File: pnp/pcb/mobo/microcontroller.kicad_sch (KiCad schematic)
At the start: 32 parts, among them J1 SWD Header, J32 BOOT_JUMPER, SW1 SW_Push, SW2 SW_Push, U1 STM32F407VETx, Y1 8MHz

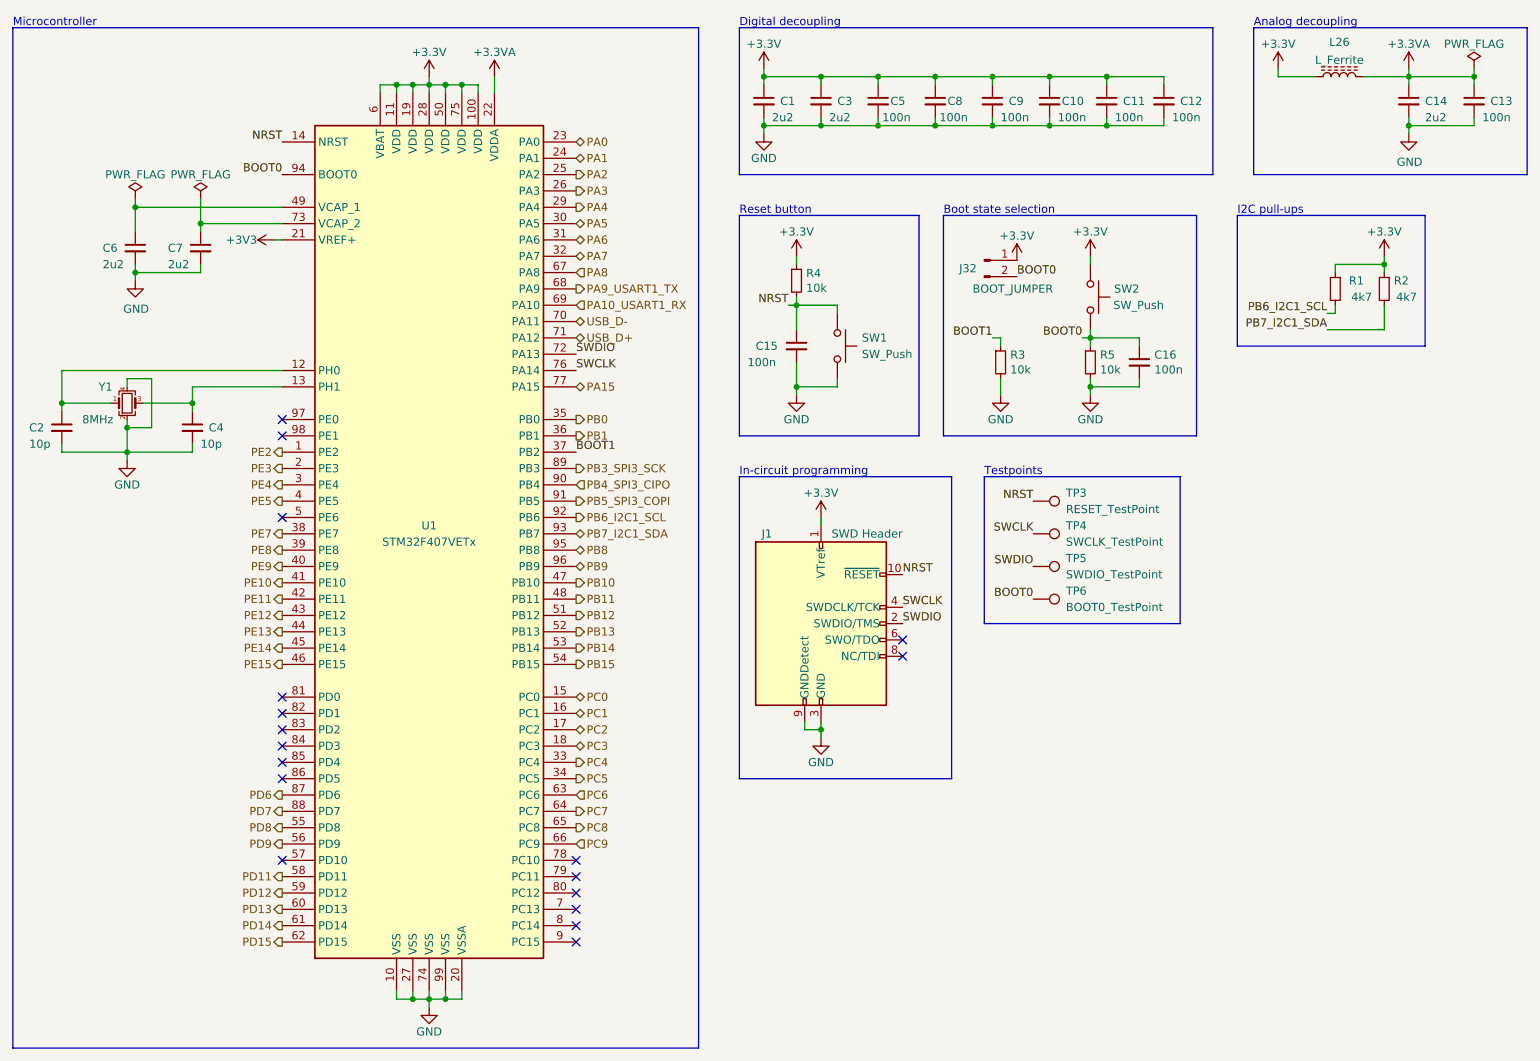
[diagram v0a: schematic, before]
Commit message: tweak PN of mobo
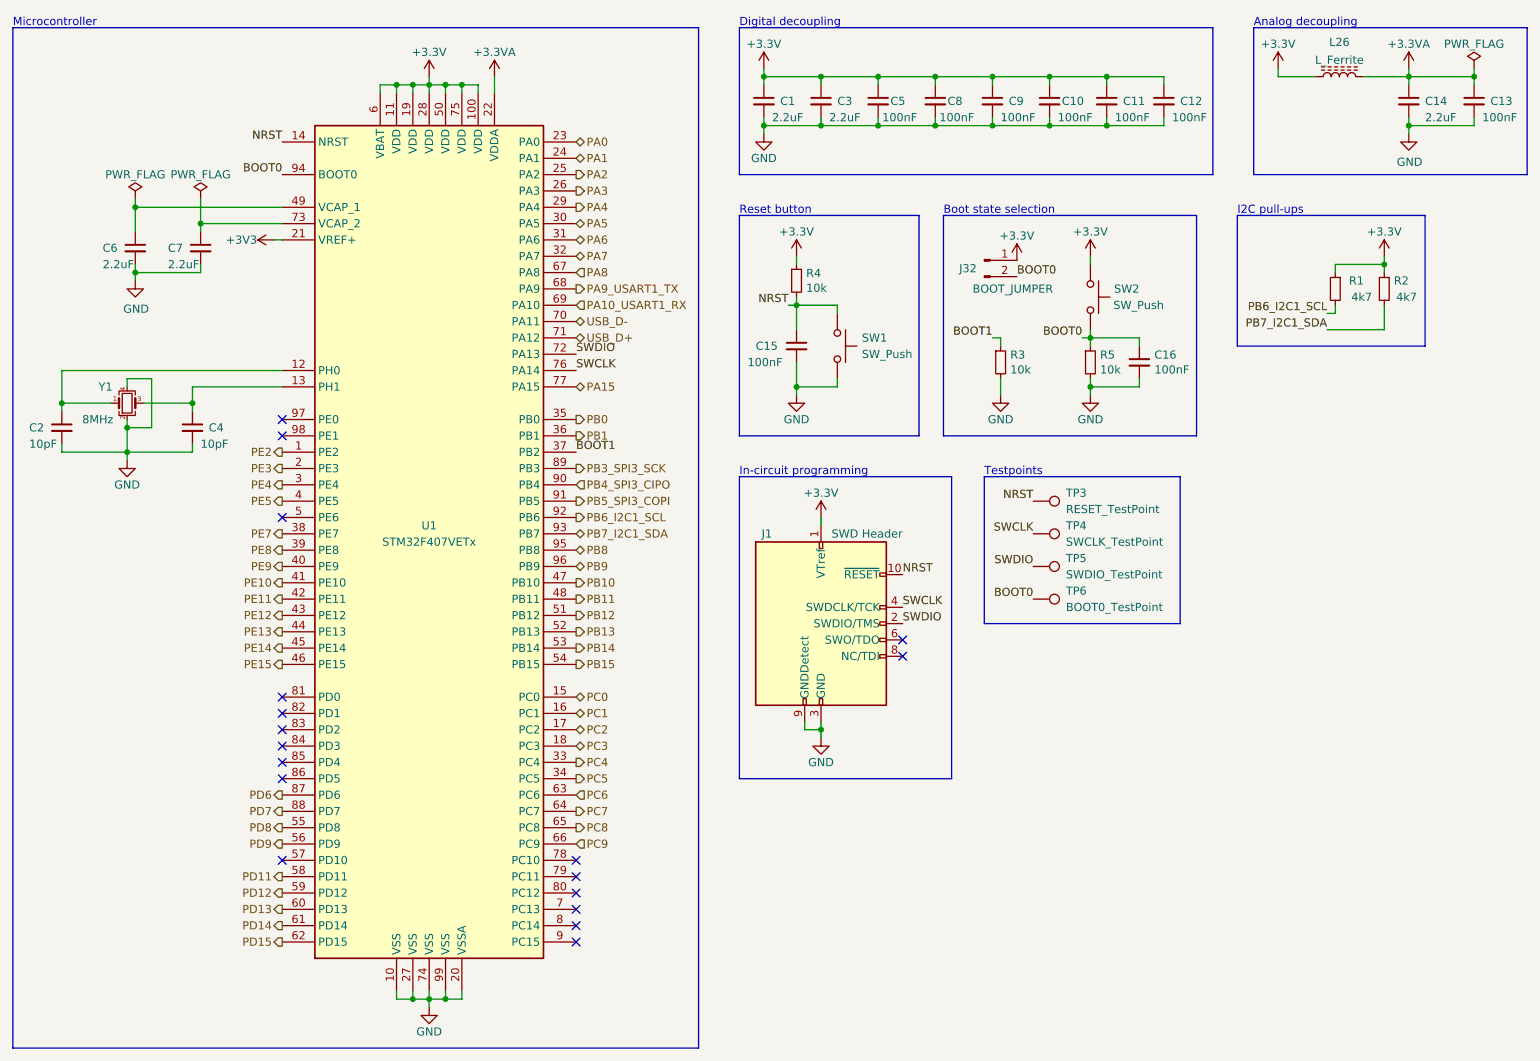
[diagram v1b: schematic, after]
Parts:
- C1, C14, C3, C6, C7: value 2u2 -> 2.2uF
- C10, C11, C12, C13, C15, C16, C5, C8, C9: value 100n -> 100nF
- C2, C4: value 10p -> 10pF
- J32: LCSC (none) -> C492401
- L26: LCSC (none) -> C79382
- TP3, TP4, TP5, TP6: LCSC (none) -> DNP
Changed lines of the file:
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@@
+      (effects (font (size 1.27 1.27)) hide)
+    )
+    (property "LCSC" "DNP" (at 182.88 116.84 0)
       (effects (font (size 1.27 1.27)) hide)
     )
@@
       (effects (font (size 1.27 1.27)) (justify left))
     )
-    (property "Value" "100n" (at 195.58 41.91 0)
+    (property "Value" "100nF" (at 195.58 41.91 0)
       (effects (font (size 1.27 1.27)) (justify left))
     )
@@
       (effects (font (size 1.27 1.27)) (justify left))
     )
-    (property "Value" "100n" (at 204.47 41.91 0)
+    (property "Value" "100nF" (at 204.47 41.91 0)
       (effects (font (size 1.27 1.27)) (justify left))
     )
@@
       (effects (font (size 1.27 1.27)) (justify left))
     )
-    (property "Value" "2u2" (at 142.24 41.91 0)
+    (property "Value" "2.2uF" (at 142.24 41.91 0)
       (effects (font (size 1.27 1.27)) (justify left))
     )
@@
       (effects (font (size 1.27 1.27)) (justify left))
     )
-    (property "Value" "100n" (at 138.43 80.01 0)
+    (property "Value" "100nF" (at 138.43 80.01 0)
       (effects (font (size 1.27 1.27)) (justify left))
     )
@@
       (effects (font (size 1.27 1.27)) (justify left))
     )
-    (property "Value" "2u2" (at 38.1 64.77 0)
+    (property "Value" "2.2uF" (at 38.1 64.77 0)
       (effects (font (size 1.27 1.27)) (justify left))
     )
@@
       (effects (font (size 1.27 1.27)) (justify left))
     )
-    (property "Value" "100n" (at 168.275 41.91 0)
+    (property "Value" "100nF" (at 168.275 41.91 0)
       (effects (font (size 1.27 1.27)) (justify left))
     )
@@
       (effects (font (size 1.27 1.27)) hide)
     )
+    (property "LCSC" "DNP" (at 182.88 101.6 0)
+      (effects (font (size 1.27 1.27)) hide)
+    )
     (pin "1")
     (instances
@@
       (effects (font (size 1.27 1.27)) (justify left))
     )
-    (property "Value" "100n" (at 177.8 41.91 0)
+    (property "Value" "100nF" (at 177.8 41.91 0)
       (effects (font (size 1.27 1.27)) (justify left))
     )
@@
       (effects (font (size 1.27 1.27)) (justify left))
     )
-    (property "Value" "100n" (at 186.69 41.91 0)
+    (property "Value" "100nF" (at 186.69 41.91 0)
       (effects (font (size 1.27 1.27)) (justify left))
     )
@@
       (effects (font (size 1.27 1.27)) (justify left))
     )
-    (property "Value" "100n" (at 159.385 41.91 0)
+    (property "Value" "100nF" (at 159.385 41.91 0)
       (effects (font (size 1.27 1.27)) (justify left))
     )
@@
       (effects (font (size 1.27 1.27)) (justify left))
     )
-    (property "Value" "2u2" (at 243.84 41.91 0)
+    (property "Value" "2.2uF" (at 243.84 41.91 0)
       (effects (font (size 1.27 1.27)) (justify left))
     )
@@
     )
     (property "Datasheet" "~" (at 175.26 64.135 0)
+      (effects (font (size 1.27 1.27)) hide)
+    )
+    (property "LCSC" "C492401" (at 175.26 64.135 0)
       (effects (font (size 1.27 1.27)) hide)
     )
@@
       (effects (font (size 1.27 1.27)) hide)
     )
+    (property "LCSC" "C79382" (at 230.505 35.56 0)
+      (effects (font (size 1.27 1.27)) hide)
+    )
     (pin "1")
     (pin "2")
@@
       (effects (font (size 1.27 1.27)) (justify left))
     )
-    (property "Value" "10p" (at 53.34 92.71 0)
+    (property "Value" "10pF" (at 53.34 92.71 0)
       (effects (font (size 1.27 1.27)) (justify left))
     )
@@
       (effects (font (size 1.27 1.27)) (justify left))
     )
-    (property "Value" "2u2" (at 151.13 41.91 0)
+    (property "Value" "2.2uF" (at 151.13 41.91 0)
       (effects (font (size 1.27 1.27)) (justify left))
     )
@@
       (effects (font (size 1.27 1.27)) (justify left))
     )
-    (property "Value" "100n" (at 201.7268 81.153 0)
+    (property "Value" "100nF" (at 201.7268 81.153 0)
       (effects (font (size 1.27 1.27)) (justify left))
     )
@@
       (effects (font (size 1.27 1.27)) (justify left))
     )
-    (property "Value" "100n" (at 252.73 41.91 0)
+    (property "Value" "100nF" (at 252.73 41.91 0)
       (effects (font (size 1.27 1.27)) (justify left))
     )
@@
       (effects (font (size 1.27 1.27)) hide)
     )
+    (property "LCSC" "DNP" (at 182.88 106.68 0)
+      (effects (font (size 1.27 1.27)) hide)
+    )
     (pin "1")
     (instances
@@
       (effects (font (size 1.27 1.27)) (justify left))
     )
-    (property "Value" "2u2" (at 48.26 64.77 0)
+    (property "Value" "2.2uF" (at 48.26 64.77 0)
       (effects (font (size 1.27 1.27)) (justify left))
     )
@@
       (effects (font (size 1.27 1.27)) (justify left))
     )
-    (property "Value" "10p" (at 26.67 92.71 0)
+    (property "Value" "10pF" (at 26.67 92.71 0)
       (effects (font (size 1.27 1.27)) (justify left))
     )
@@
       (effects (font (size 1.27 1.27)) hide)
     )
+    (property "LCSC" "DNP" (at 182.88 111.76 0)
+      (effects (font (size 1.27 1.27)) hide)
+    )
